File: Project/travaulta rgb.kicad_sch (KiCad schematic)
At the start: 27 parts, among them J5 ARGB, SW38 BOOT0, U1 STM32F401CBUx, U2 XC6206PxxxMR, Y1 8 MHz

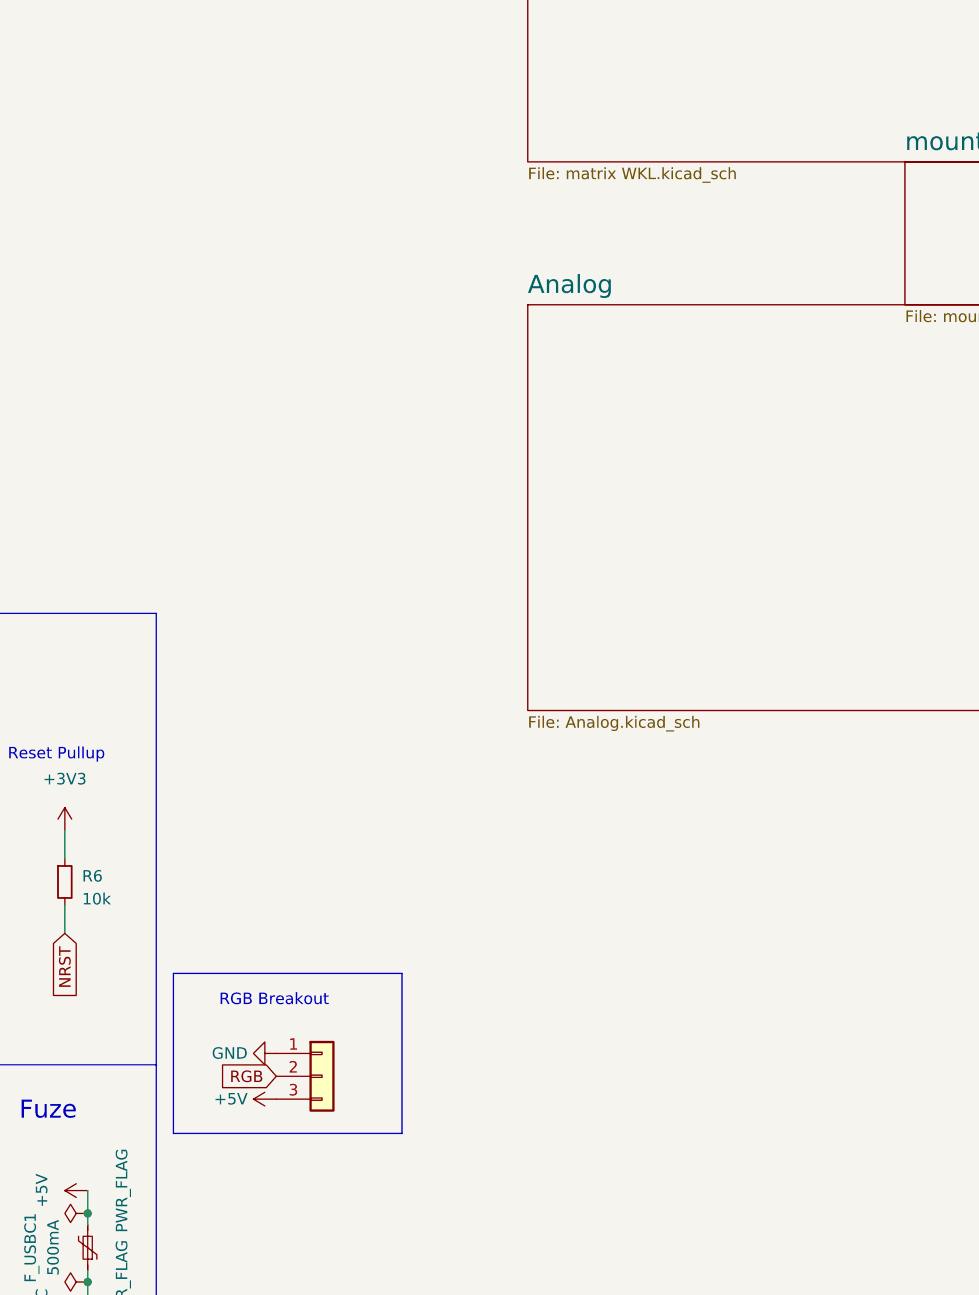
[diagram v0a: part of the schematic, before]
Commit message: added rgb breakout to HHKB&WKL
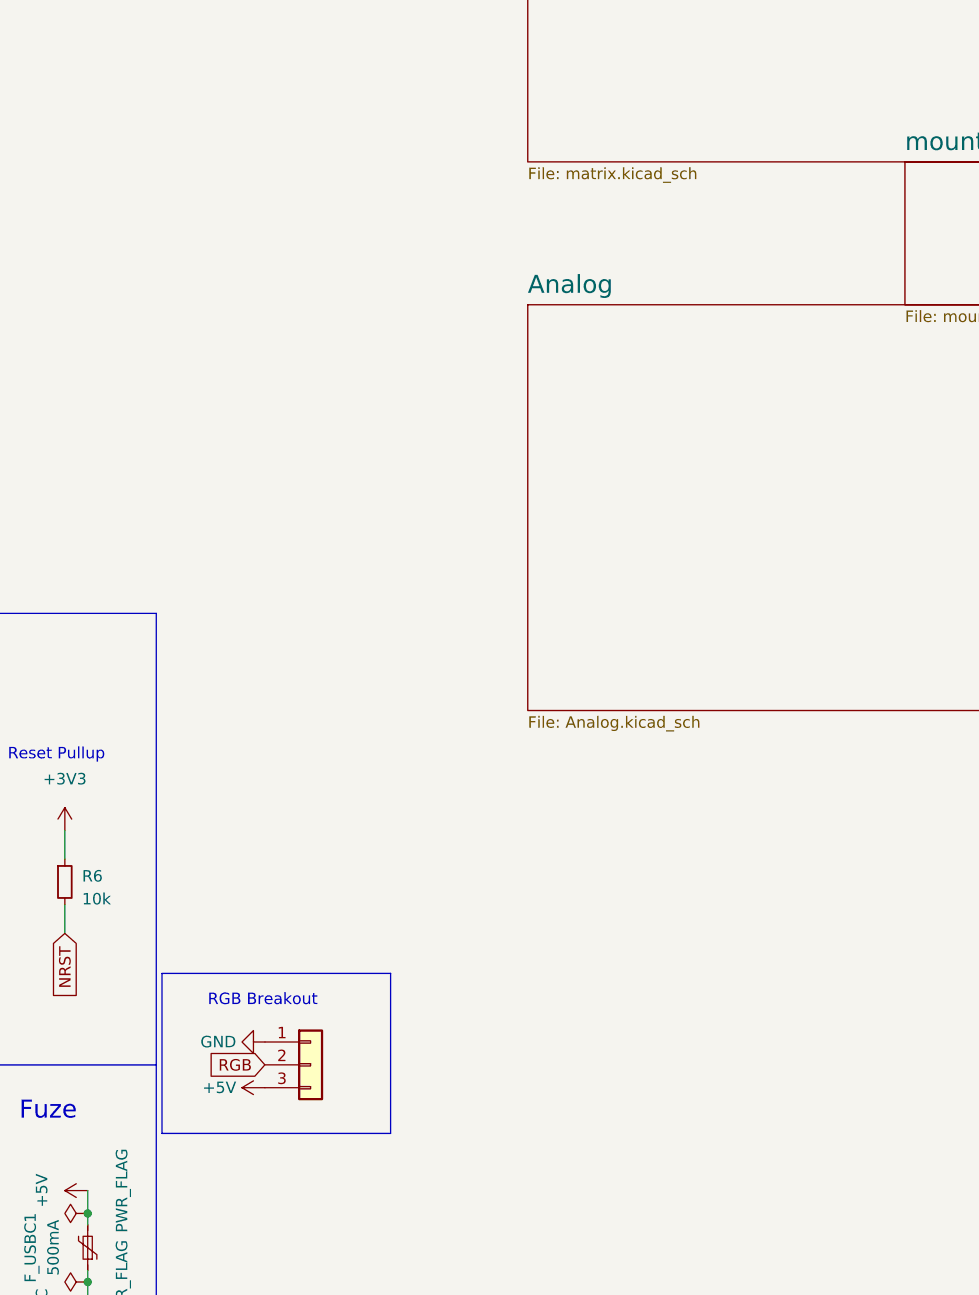
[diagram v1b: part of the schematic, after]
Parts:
- J5: footprint cipulot_parts:PinHeader_RGB strip -> Connector_PinHeader_1.27mm:PinHeader_1x03_P1.27mm_Vertical
- USB1: footprint cipulot_parts:XUNPU-TYPEC-312DSS-ACP16-Assembly -> cipulot_parts:TYPEC-304YSSW-ACP16
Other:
- sheet matrix: file matrix WKL.kicad_sch -> matrix.kicad_sch
